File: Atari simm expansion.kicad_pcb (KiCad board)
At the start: 2 copper layers, 113.2 x 55.8 mm, 27 parts, among them J1 4464_A, J2 4464_B, J3 4464_A, J4 4464_B, J5 SMMU_A, J6 SMMU_B, J7 MMU_A, J8 MMU_A, J9 Mem_On_Off, U1 SIMM_exp_GAL, U11 DRAM_1MB_4bit, U12 DRAM_1MB_4bit, U2 74LS175, U3 74LS157, U4 MMU

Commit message: Tracking
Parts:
- added J10: PB0..7, Connector_PinHeader_2.54mm:PinHeader_1x08_P2.54mm_Vertical, F.Cu at (149.8, 110.3)
- added J11: RAS_sel, Connector_PinHeader_2.00mm:PinHeader_2x04_P2.00mm_Vertical, F.Cu at (131.3, 90.7)
- added U13: 74LS04, Package_SO:SOIC-14_3.9x8.7mm_P1.27mm, F.Cu at (143.9, 88.6)
- moved C4 69.8 mm to (105.0, 117.3), turned to 270 degrees
- moved C3 60.0 mm to (105.0, 108.6), turned to 270 degrees
- moved C2 51.3 mm to (123.4, 103.1), turned to 90 degrees
- moved C1 48.2 mm to (118.8, 108.5), turned to 270 degrees
- moved R6 43.0 mm to (143.5, 109.7), turned to 270 degrees
- moved R7 39.3 mm to (145.8, 109.7), turned to 270 degrees
- moved J9 36.4 mm to (140.4, 111.1), turned to 180 degrees
- moved C5 31.5 mm to (144.2, 102.9), turned to 90 degrees
- moved R1 30.2 mm to (180.5, 110.9), turned to 270 degrees
- moved R4 26.6 mm to (173.2, 110.8), turned to 270 degrees
- moved R3 23.2 mm to (175.6, 110.8), turned to 270 degrees
- moved R2 21.6 mm to (178.1, 110.9), turned to 270 degrees
- moved R5 20.3 mm to (170.7, 110.8), turned to 270 degrees
- moved U3 4.01 mm to (125.6, 110.1)
- moved U2 2.26 mm to (111.9, 110.2)
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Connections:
- net A11 renamed A11a
- net A12 renamed A12a
- net A13 renamed A13a
- net REN renamed PB0
- J1 pad 6: A6 -> (no net)
- J1 pad 7: A5 -> (no net)
- J1 pad 8: A4 -> (no net)
- J2 pad 5: A0 -> (no net)
- J2 pad 6: A1 -> (no net)
- J2 pad 7: A2 -> (no net)
- J2 pad 8: A3 -> (no net)
- J4 pad 3: CAS -> (no net)
- J4 pad 9: A7 -> (no net)
- J7 pad 10: GND -> GNDa
- J7 pad 4: A14 -> A14a
- J7 pad 5: A15 -> A15a
- J7 pad 6: (no net) -> PB7
- J8 pad 3: (no net) -> PB1
- U3 pad 10: VCC -> GND
- U3 pad 11: VCC -> GND
- U4 pad 10: GND -> GNDa
- U4 pad 4: A14 -> A14a
- U4 pad 5: A15 -> A15a
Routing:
- net GND: track 0.00 -> 230.1 mm, vias 0 -> 13
- net VCC: track 0.00 -> 189.3 mm, vias 0 -> 3
- net REF: track 0.00 -> 118.3 mm
- net PB7: track 0.00 -> 117.1 mm, vias 0 -> 4
- net PB1: track 0.00 -> 109.3 mm, vias 0 -> 1
- net MAP: track 0.00 -> 106.4 mm, vias 0 -> 2
- net BE: track 0.00 -> 96.8 mm, vias 0 -> 1
- net PB4: track 0.00 -> 90.3 mm, vias 0 -> 1
- net PB3: track 0.00 -> 84.0 mm, vias 0 -> 2
- net PB2: track 0.00 -> 82.8 mm, vias 0 -> 1
- net PB5: track 0.00 -> 78.1 mm, vias 0 -> 1
- net RAS: track 0.00 -> 77.4 mm, vias 0 -> 3
- net A7: track 0.00 -> 71.1 mm, vias 0 -> 1
- net PB0: track 0.00 -> 68.8 mm, vias 0 -> 1
- net CAS: track 0.00 -> 67.9 mm, vias 0 -> 1
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
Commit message: Finished
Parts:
- moved J11 13.6 mm to (144.9, 91.6), turned to 180 degrees
- moved U13 8.43 mm to (135.4, 88.6)
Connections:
- J1 pad 5: (no net) -> RAS
- J11 pad 1: Net-(J11-Pad1) -> RAS_OUT
- J11 pad 2: Net-(J11-Pad2) -> RAS
- J11 pad 3: Net-(J11-Pad3) -> RAS_OUT
- J11 pad 5: Net-(J11-Pad5) -> RAS_OUT
- J11 pad 7: Net-(J11-Pad7) -> RAS_OUT
- J2 pad 9: A7 -> (no net)
- J3 pad 5: RAS -> (no net)
- J4 pad 9: (no net) -> A7
- J8 pad 1: VCC -> VCCa
- R1 pad 1: VCC -> VCCa
- R2 pad 1: VCC -> VCCa
- R3 pad 1: VCC -> VCCa
- R4 pad 1: VCC -> VCCa
- R5 pad 1: VCC -> VCCa
- U1 pad 1: RAS -> RAS_OUT
- U11 pad 4: RAS -> RAS_OUT
- U12 pad 4: RAS -> RAS_OUT
- U13 pad 1: (no net) -> RAS
- U13 pad 10: Net-(J11-Pad4) -> Net-(U13-Pad10)
- U13 pad 14: (no net) -> VCC
- U13 pad 7: (no net) -> GND
- U13 pad 8: (no net) -> Net-(J11-Pad4)
- U13 pad 9: Net-(J11-Pad4) -> Net-(U13-Pad10)
- U3 pad 1: RAS -> RAS_OUT
- U4 pad 20: VCC -> VCCa
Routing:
- net RAS_OUT: track 0.00 -> 101.9 mm, vias 0 -> 4
- net RAS: track 77.4 -> 36.7 mm, vias 3 -> 0
- net VCCa: track 0.00 -> 22.8 mm
- net VCC: track 189.3 -> 176.0 mm
- net A7: track 71.1 -> 58.2 mm, vias 1 -> 2
- net Net-(J11-Pad6): track 0.00 -> 11.9 mm
- net Net-(J11-Pad8): track 0.00 -> 10.9 mm, vias 0 -> 1
- net Net-(U13-Pad13): track 0.00 -> 9.56 mm
- net Net-(J11-Pad4): track 0.00 -> 5.94 mm
- net GND: track 230.1 -> 224.3 mm, vias 13 -> 38
- net Net-(U13-Pad2): track 0.00 -> 1.27 mm
- net Net-(U13-Pad10): track 0.00 -> 1.27 mm
- net DQ0: track 41.2 -> 40.0 mm
- net DQ1: track 39.0 -> 38.2 mm
- net WR: track 58.0 -> 57.3 mm
- added copper zone on B.Cu, net GND
- added copper zone on F.Cu, net GND
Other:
- board text added: "1MB"
- board text added: "OFF"
- board text added: "PB0"
- board text added: "PB1"
- board text added: "PB2"
- board text added: "PB3"
- board text added: "PB4"
- board text added: "PB5"
- board text added: "PB6"
- board text added: "PB7"
- board text added: "RAS"
- board text added: "RAS1"
- board text added: "RAS2"
- board text added: "RAS3"

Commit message: Gerber files
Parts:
- moved U4 0.50 mm to (190.4, 116.0)
- moved J7 0.38 mm to (190.4, 113.4)
- moved J8 0.38 mm to (190.4, 105.8)
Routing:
- net GND: track 224.3 -> 146.5 mm, vias 38 -> 40
- net RAS_OUT: track 101.9 -> 100.8 mm
- net PB0: track 68.8 -> 69.7 mm
- net VCC: track 176.0 -> 176.7 mm
- net PB1: track 109.3 -> 110.0 mm
- net DQ3: track 41.9 -> 41.3 mm
- net PB7: track 117.1 -> 117.6 mm
- net MAP: track 106.4 -> 106.9 mm
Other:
- board size 113.2 x 55.8 mm -> 112.8 x 55.8 mm

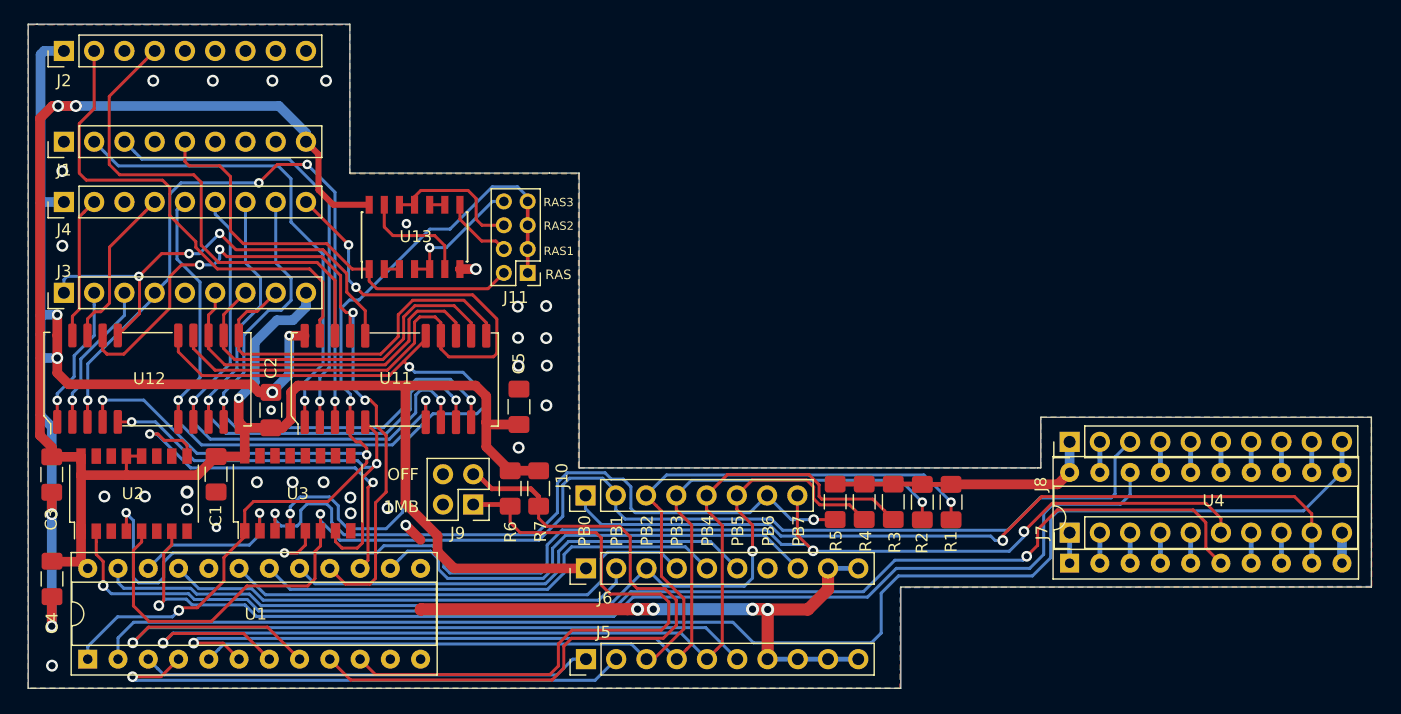
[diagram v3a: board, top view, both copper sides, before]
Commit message: Text on board
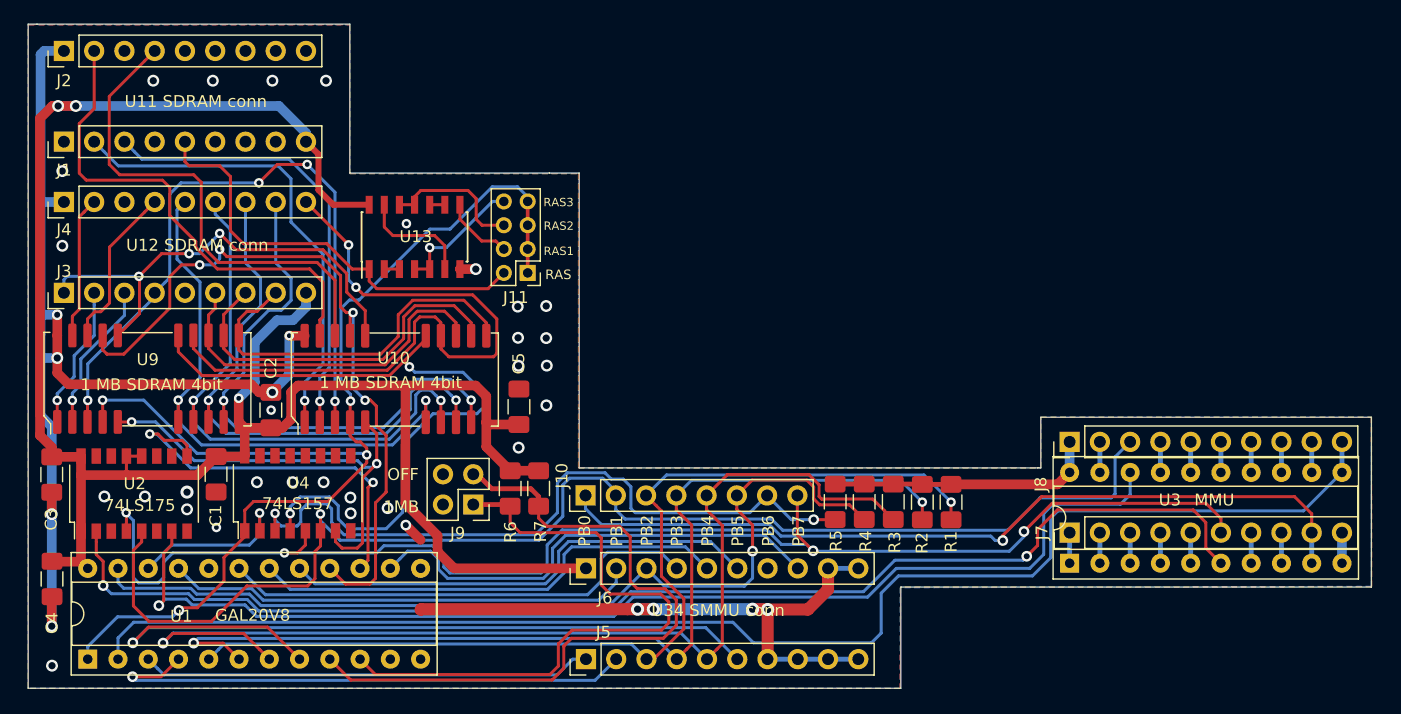
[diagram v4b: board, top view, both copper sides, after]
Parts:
- renumbered U11 to U10, U4 to U3, U3 to U4, U12 to U9
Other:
- board text added: "1 MB SDRAM 4bit"
- board text added: "74LS157"
- board text added: "74LS175"
- board text added: "GAL20V8"
- board text added: "MMU"
- board text added: "U11 SDRAM conn"
- board text added: "U12 SDRAM conn"
- board text added: "U34 SMMU conn"

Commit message: Tracking
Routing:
- net HALT: track 39.9 -> 37.3 mm
- net PB7: track 117.6 -> 115.1 mm
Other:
- outline, holes or cut-outs redrawn
